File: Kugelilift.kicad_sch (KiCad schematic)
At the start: 7 parts, among them J1 I2C, J4 Conn_01x05, U1 WeMos_D1_mini, U2 TCRT5000, U3 ULN2003A

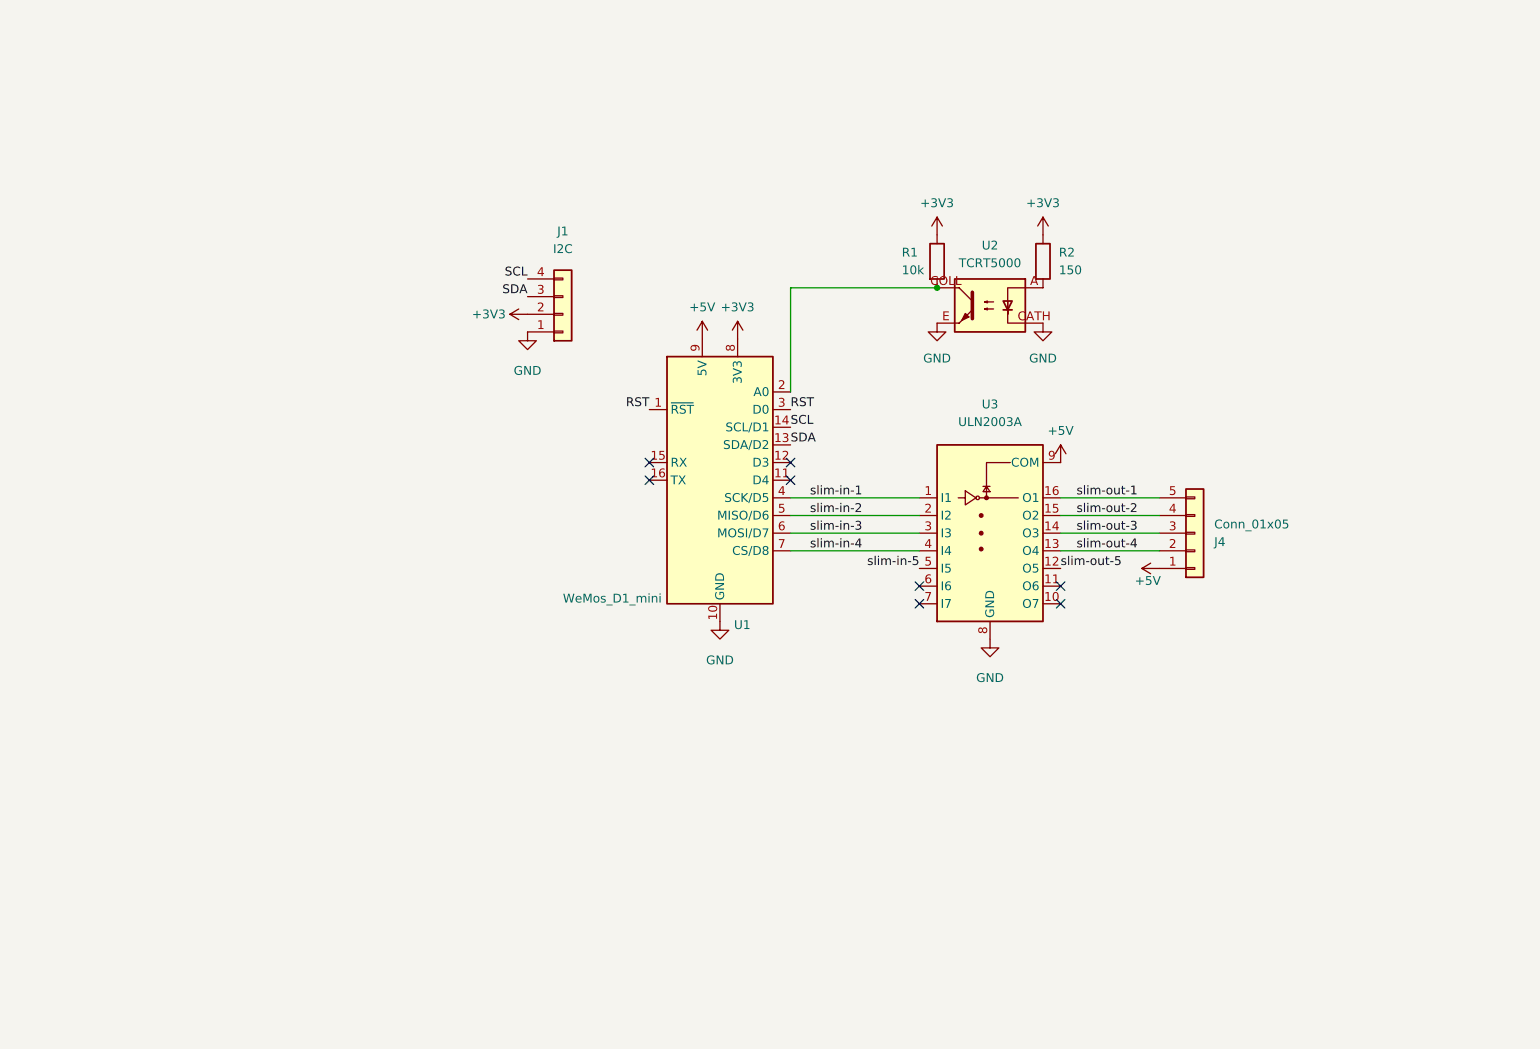
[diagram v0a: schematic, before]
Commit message: Working progres with SMT ESP12 module
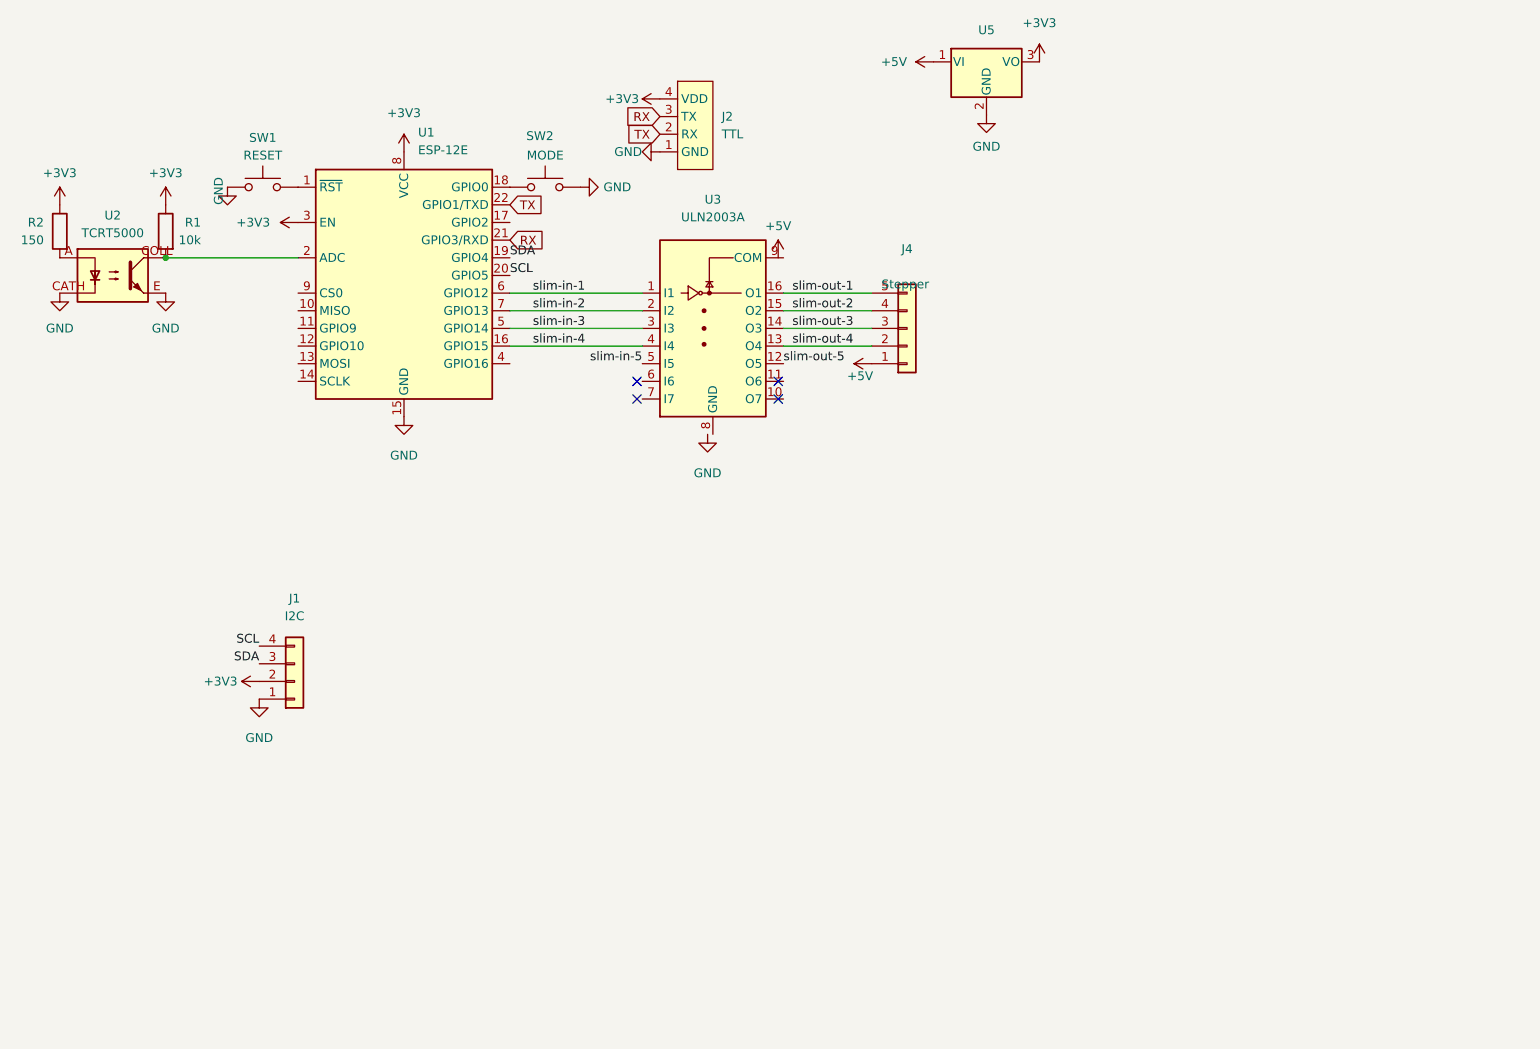
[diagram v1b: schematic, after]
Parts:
- removed U1: WeMos_D1_mini, Module:WEMOS_D1_mini_light, symbol MCU_Module:WeMos_D1_mini
- added J2: TTL, Connector_PinHeader_2.54mm:PinHeader_1x04_P2.54mm_Vertical, symbol ftdi-connector:TTL
- added SW1: RESET, Button_Switch_SMD:SW_Push_1P1T_NO_Vertical_Wuerth_434133025816, symbol Switch:SW_Push
- added SW2: MODE, Button_Switch_SMD:SW_Push_1P1T_NO_Vertical_Wuerth_434133025816, symbol Switch:SW_Push
- added U1: ESP-12E, RF_Module:ESP-12E, symbol RF_Module:ESP-12E
- added U5: UA78M33_TO252, Package_TO_SOT_SMD:TO-252-2, symbol Regulator_Linear:KA78M05_TO252
- J4: value Conn_01x05 -> Stepper
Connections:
- net +3V3: now also J2.4 (VDD), U1.3 (EN), U1.8 (VCC), U5.3 (VO)
- net +5V: now also U5.1 (VI); no longer U3.9 (COM)
- net GND: now also J2.1 (GND), SW1.1, SW2.1, U1.15 (GND), U5.2 (GND); no longer U3.8 (GND)
- net SCL: now also U1.20 (GPIO5)
- net SDA: now also U1.19 (GPIO4)
- net slim-in-1: now also U1.6 (GPIO12)
- net slim-in-2: now also U1.7 (GPIO13)
- net slim-in-3: now also U1.5 (GPIO14)
- net slim-in-4: now also U1.16 (GPIO15)
- net at R1.2, U2.COLL: now also U1.2 (ADC)
- new net: SW2.2, U1.18 (GPIO0)
- new net: SW1.2, U1.1 (~{RST})
- new net RX: J2.3 (TX), U1.21 (GPIO3/RXD)
- new net TX: J2.2 (RX), U1.22 (GPIO1/TXD)
- no-connect marks 8 -> 4
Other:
- moved on the sheet: J1, J4, R1, R2, U2, U3

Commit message: ESP-01F based PCB
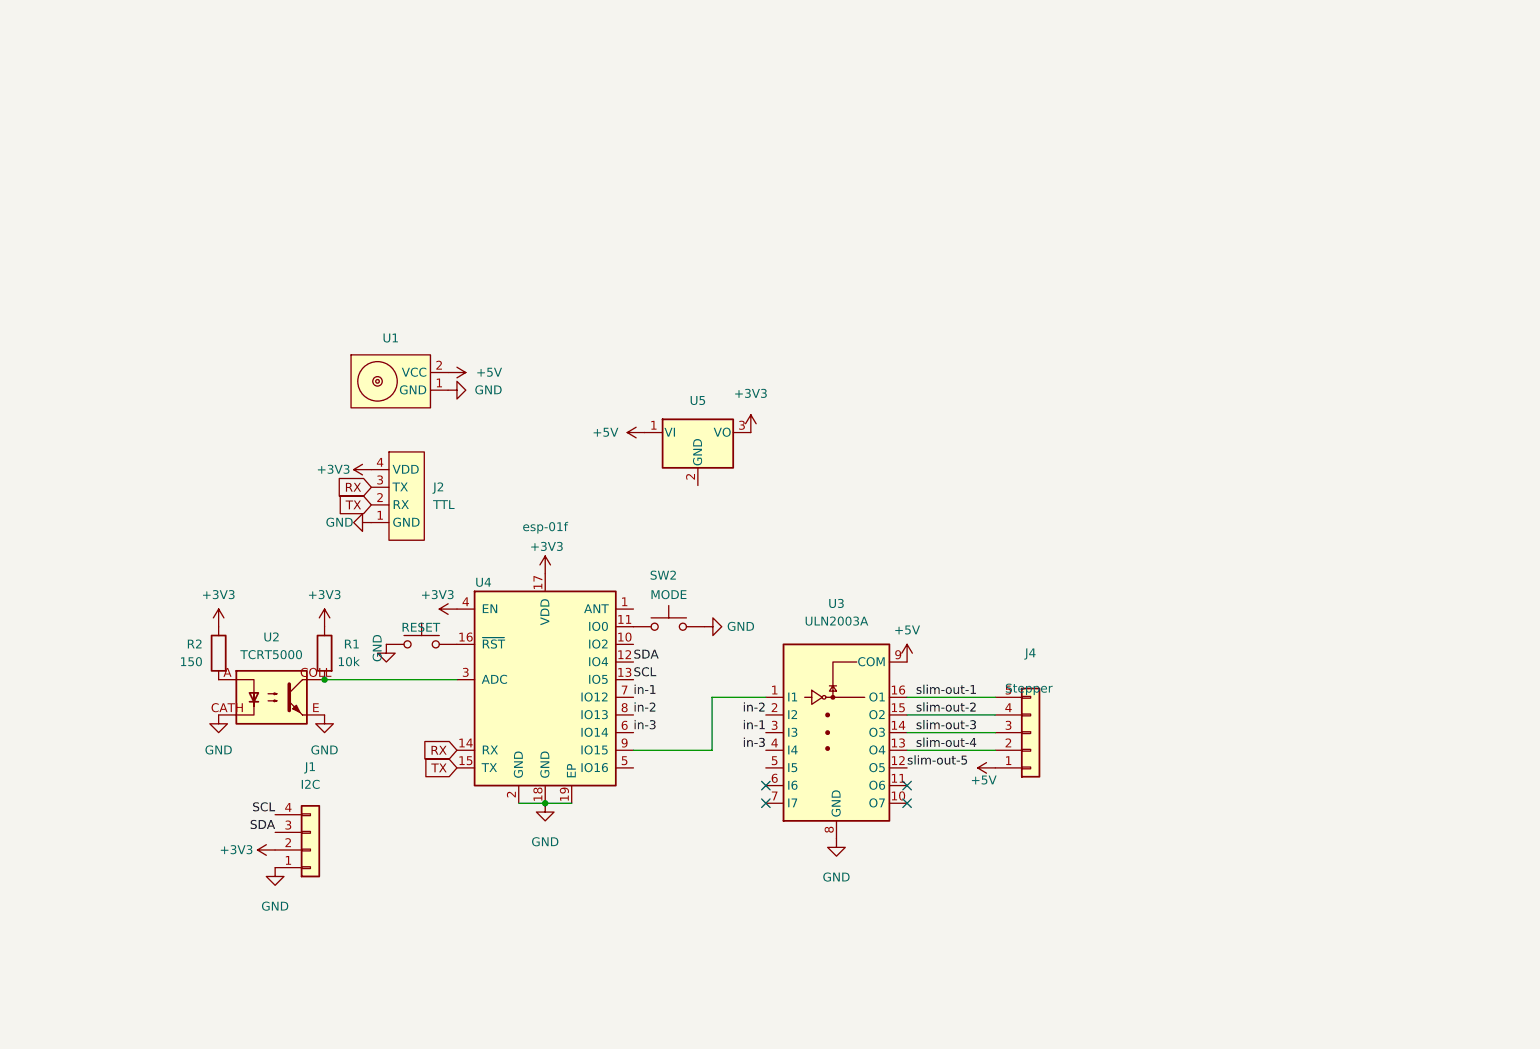
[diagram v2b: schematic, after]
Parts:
- removed U1: ESP-12E, RF_Module:ESP-12E, symbol RF_Module:ESP-12E
- added U1: magnetic-charger, magnetic-charger:magnetic-charger, symbol magnetic-charger:magnetic-charger
- added U4: esp-01f, esp-01f:esp-01f, symbol esp-01f:esp-01f
- J4: footprint Connector_JST:JST_EH_S5B-EH_1x05_P2.50mm_Horizontal -> Connector_JST:JST_EH_B5B-EH-A_1x05_P2.50mm_Vertical
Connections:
- net +3V3: now also U4.17 (VDD), U4.4 (EN)
- net +5V: now also U3.9 (COM), U1.2 (VCC)
- net GND: now also U3.8 (GND), U1.1 (GND), U4.18 (GND), U4.19 (EP), U4.2 (GND); no longer U5.2 (GND)
- net RX: now also U4.14 (RX)
- net SCL: now also U4.13 (IO5)
- net SDA: now also U4.12 (IO4)
- net TX: now also U4.15 (TX)
- net at SW2.2: now also U4.11 (IO0)
- net at SW1.2: now also U4.16 (~{RST})
- net at R1.2, U2.COLL: now also U4.3 (ADC)
- net slim-in-1: no longer names the net of U3.1 (I1)
- net slim-in-1: now also U4.9 (IO15)
- net slim-in-2 renamed in-2
- net in-2: now also U4.8 (IO13)
- net slim-in-3 renamed in-1
- net in-1: now also U4.7 (IO12)
- net slim-in-4 renamed in-3
- net in-3: now also U4.6 (IO14)
- net slim-in-5: no longer names the net of U3.5 (I5)
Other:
- moved on the sheet: J1, J2, J4, R1, R2, SW2, U2, U3, U5

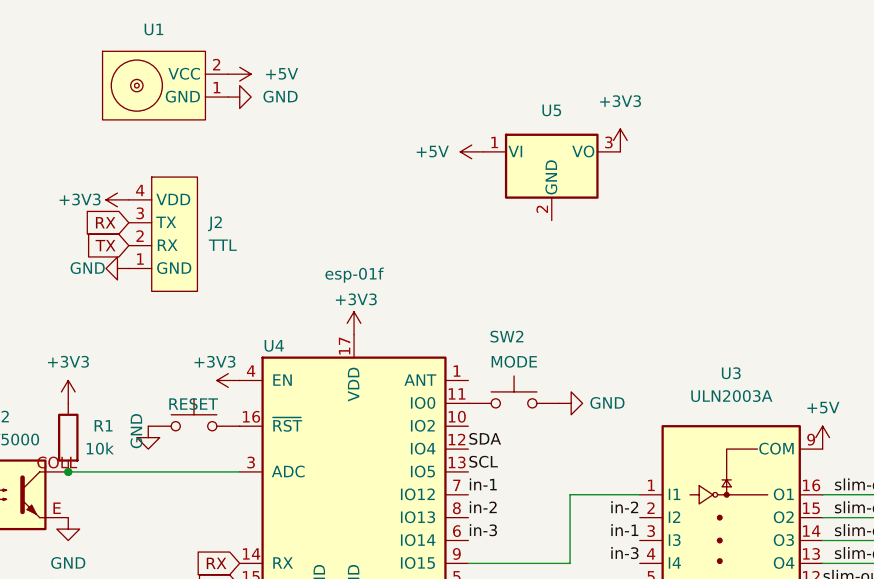
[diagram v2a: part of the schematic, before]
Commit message: PCB Version 2.2
- ESP-12F
- Linear regulator + Capacitors
- ULN2003 in small SOP-16 package
- TTL instead of USB
- TCRT5000
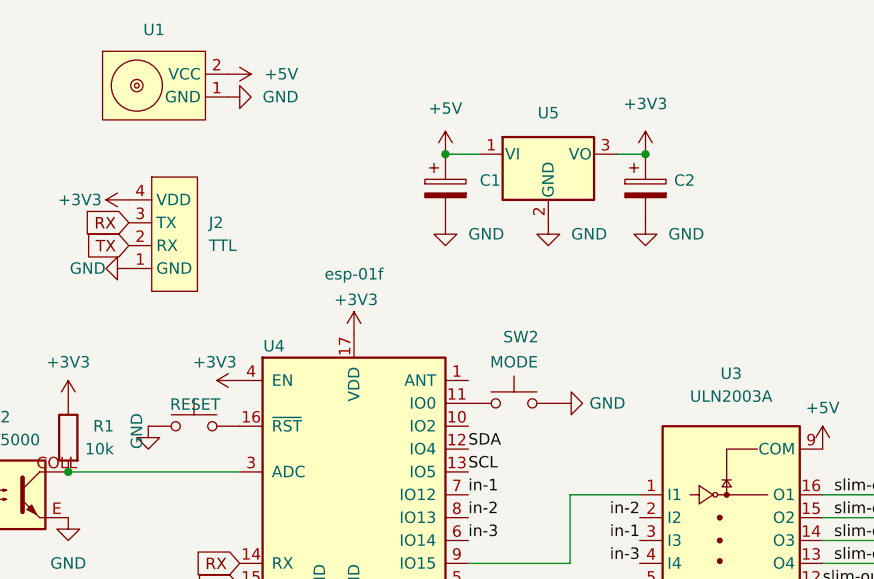
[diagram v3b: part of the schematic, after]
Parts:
- added C1, C2: C_Polarized, Capacitor_THT:CP_Radial_D6.3mm_P2.50mm, symbol Device:C_Polarized
- SW1, SW2: footprint Button_Switch_SMD:SW_Push_1P1T_NO_Vertical_Wuerth_434133025816 -> Connector_PinHeader_2.54mm:PinHeader_1x03_P2.54mm_Vertical
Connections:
- net +3V3: now also C2.1
- net +5V: now also C1.1
- net GND: now also SW1.2, SW2.2, U5.2 (GND), C1.2, C2.2; no longer SW1.1, SW2.1
- net at U4.11 (IO0): now also SW2.1; no longer SW2.2
- net at U4.16 (~{RST}): now also SW1.1; no longer SW1.2
